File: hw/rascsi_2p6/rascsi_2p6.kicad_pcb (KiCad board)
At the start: 2 copper layers, 65 x 56 mm, 98 parts, among them IC1 SN74F245DWR, IC2 SN74F245DWR, IC3 SN74F245DWR, IC4 SN74F245DWR, J1 Raspberry_Pi_2_3, J2 DNP, J20 171826-4, J3 Conn_02x25_Odd_Even, J4 I2C Pinout, J5 DNP, J6 CONNFLY DB-25, J8 USB_B_Micro, J9 Conn_02x25_Odd_Even, X1 Mac, X2 Dogcow, X3 Mac, X4 Dogcow, X5 Dogcow, X6 Dogcow, X7 Pi, X8 Pi

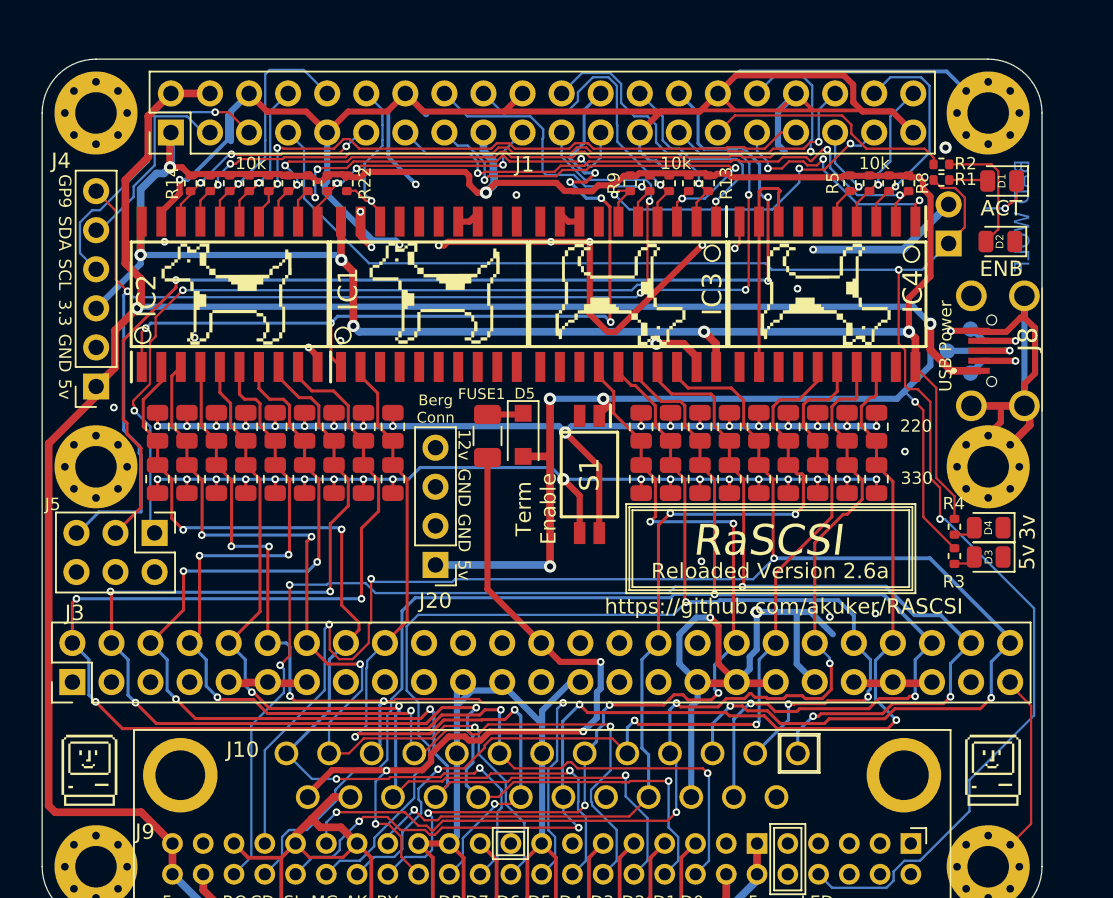
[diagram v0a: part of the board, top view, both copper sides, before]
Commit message: Updated with 74LVT245 - as ordered
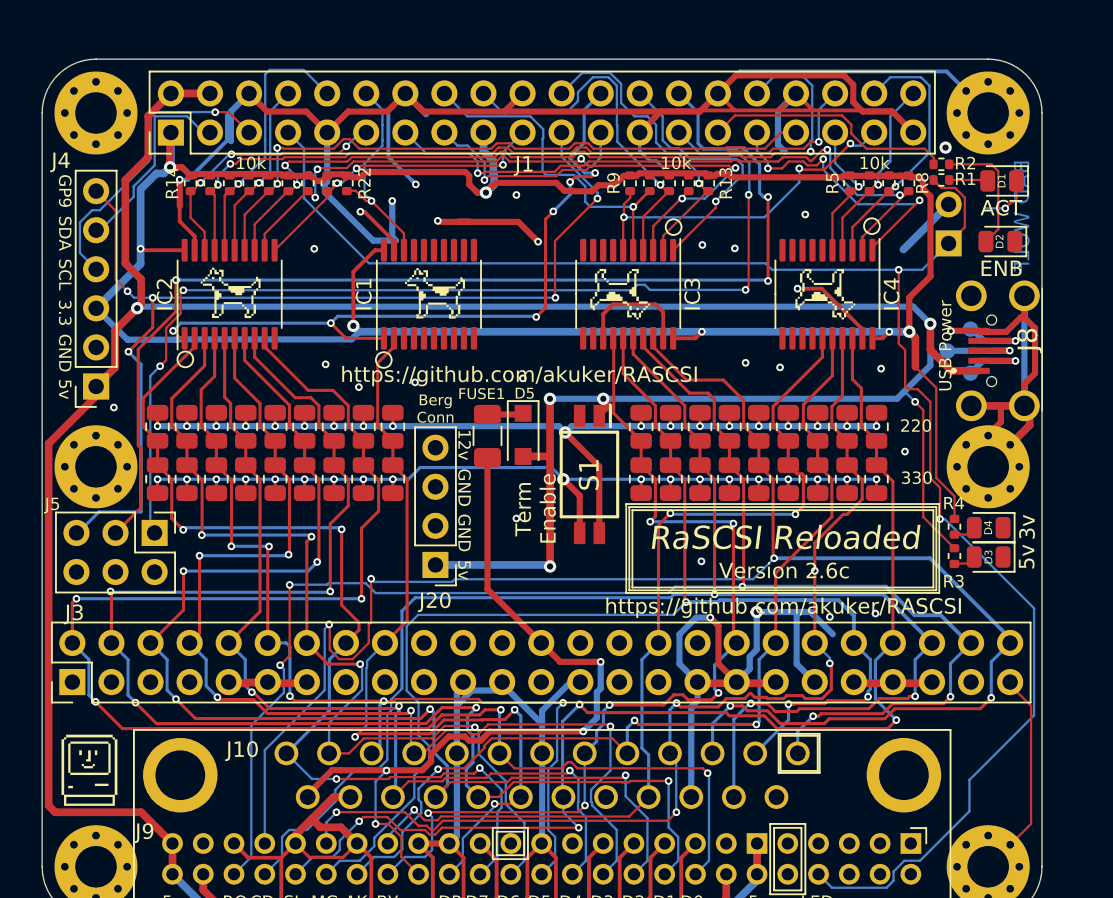
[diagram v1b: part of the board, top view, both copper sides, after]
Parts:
- removed G***: LOGO, SamacSys_Parts:mac_happy_small
- removed REF**: CE-Logo_8.5x6mm_SilkScreen, Symbol:CE-Logo_8.5x6mm_SilkScreen
- removed REF**: KiCad-Logo_5mm_SilkScreen, Symbol:KiCad-Logo_5mm_SilkScreen
- added X9: CE Logo, Symbol:CE-Logo_8.5x6mm_SilkScreen, B.Cu at (224.4, 56.1)
- IC1, IC2, IC3, IC4: value SN74F245DWR -> SN74LVT245BPWR; footprint SamacSys_Parts:SOIC127P1030X265-20N -> Package_SO:TSSOP-20_4.4x6.5mm_P0.65mm
- X2, X4, X5, X6: footprint SamacSys_Parts:dogcow -> SamacSys_Parts:dogcow_4p5mm
- moved X2 0.26 mm to (186.7, 57.7)
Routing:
- net GND: track 427.8 -> 400.3 mm, vias 28 -> 30
- net PI-DTD: track 56.2 -> 47.5 mm
- net PI_GPIO9: track 76.1 -> 67.9 mm, vias 3 -> 5
- net +3V3: track 158.3 -> 163.7 mm
- net PI-MSG: track 19.8 -> 23.2 mm
- net C-D1: track 88.3 -> 91.6 mm
- net PI-DP: track 10.9 -> 14.0 mm
- net PI-D0: track 16.8 -> 19.9 mm
- net PI-TAD: track 13.9 -> 16.9 mm
- net C-D0: track 95.6 -> 98.6 mm
- net PI-D3: track 40.0 -> 42.9 mm
- net C-D7: track 60.5 -> 63.4 mm
- net PI-IND: track 16.2 -> 19.0 mm
- net PI-I_O: track 17.2 -> 20.0 mm
- net PI-SEL: track 39.0 -> 41.8 mm
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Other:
- board text added: "RaSCSI Reloaded"
- board text added: "Version 2.6c"
- board text removed: "RaSCSI"
- board text removed: "Reloaded Version 2.6a"
